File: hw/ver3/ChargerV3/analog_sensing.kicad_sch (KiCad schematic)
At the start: 34 parts, among them U16 ADS1220xPW, U17 74HC4051PW, U18 74HC4051PW

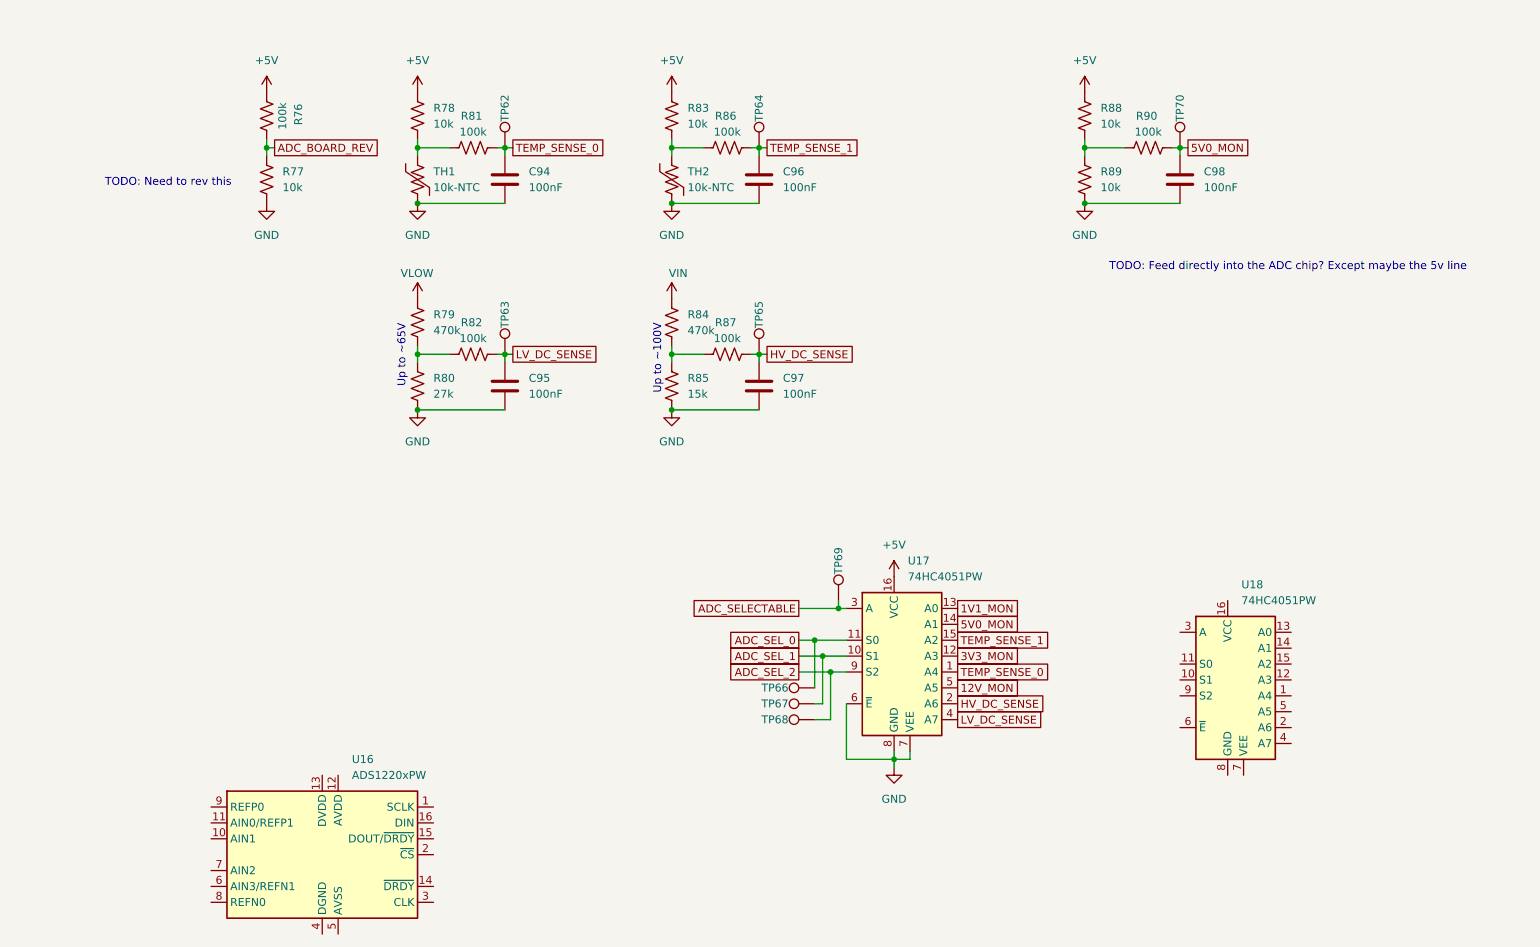
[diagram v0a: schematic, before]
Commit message: Split the design into four major components. Start working on system architecture.
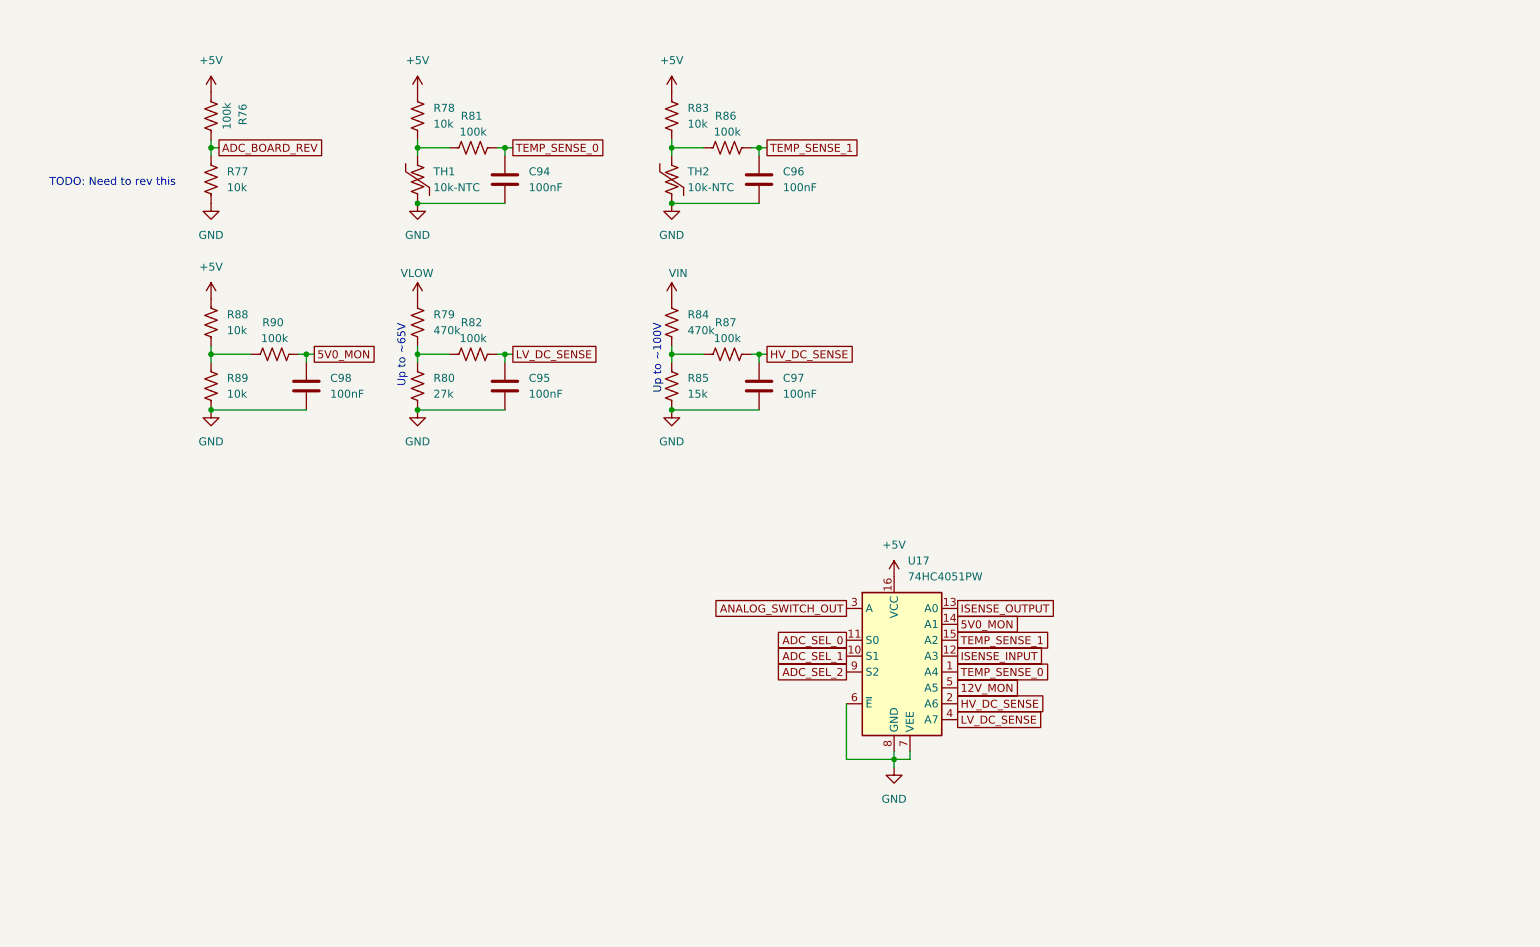
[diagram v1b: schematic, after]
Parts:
- removed TP62, TP63, TP64, TP65, TP66, TP67, TP68, TP69, TP70: TestPoint, TestPoint:TestPoint_Pad_D1.0mm, symbol Connector:TestPoint
- removed U16: ADS1220xPW, Package_SO:TSSOP-16_4.4x5mm_P0.65mm, symbol Analog_ADC:ADS1220xPW
- removed U18: 74HC4051PW, Package_SO:TSSOP-16_4.4x5mm_P0.65mm, symbol 74xx:74HC4051
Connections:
- net 1V1_MON renamed ISENSE_OUTPUT
- net 3V3_MON renamed ISENSE_INPUT
- net ADC_SELECTABLE renamed ANALOG_SWITCH_OUT
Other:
- note removed: "TODO: Feed directly into the ADC chip? Except maybe the 5v line"
- moved on the sheet: C98, R76, R77, R88, R89, R90

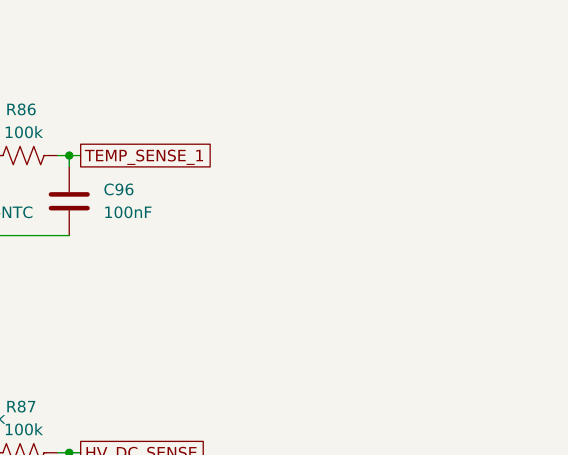
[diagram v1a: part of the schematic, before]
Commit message: Redo some charger routing. Improve design for interconnect
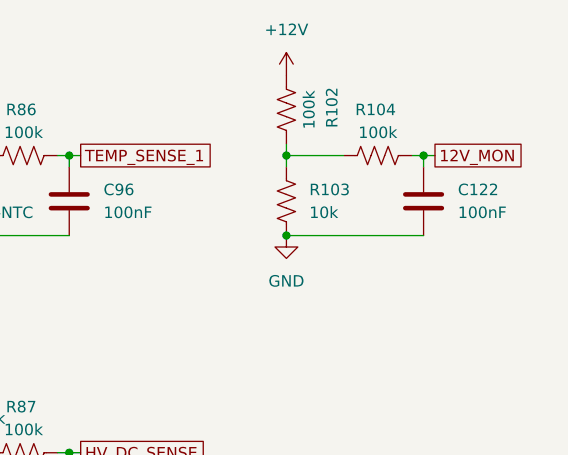
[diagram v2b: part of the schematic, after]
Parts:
- added C122: 100nF, Capacitor_SMD:C_0603_1608Metric, symbol Device:C
- added R102, R104: 100k, Resistor_SMD:R_0603_1608Metric, symbol Device:R_US
- added R103: 10k, Resistor_SMD:R_0603_1608Metric, symbol Device:R_US
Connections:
- net 12V_MON: now also C122.1, R104.2
- net GND: now also C122.2, R103.1
- new net: R102.2, R103.2, R104.1
- new net +12V: R102.1

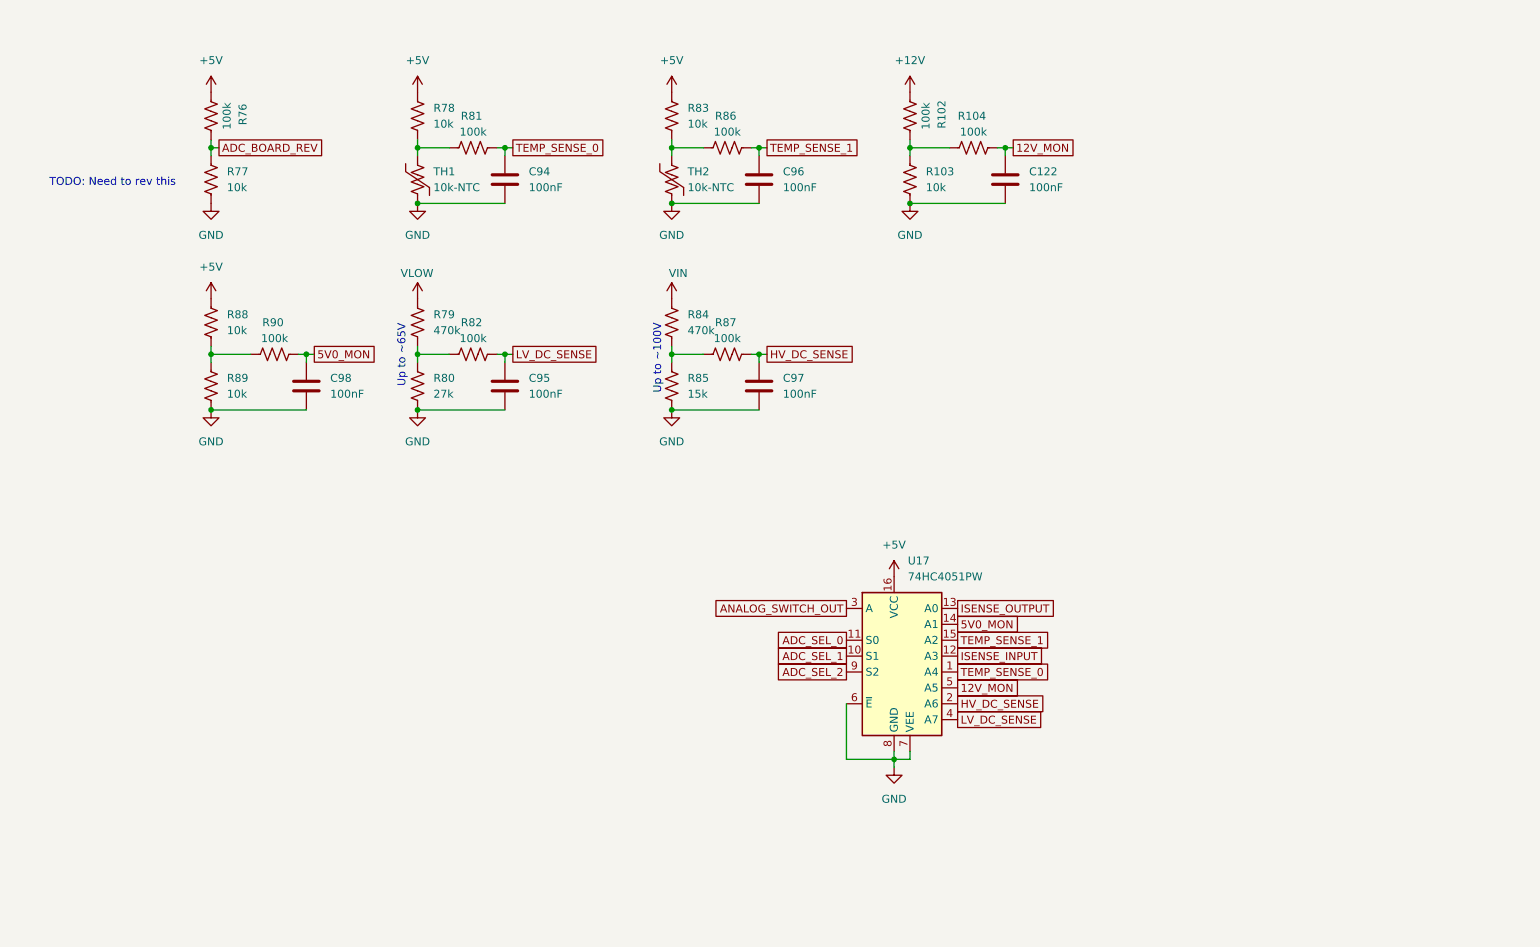
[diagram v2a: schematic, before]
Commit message: Nearly final charger schematic, updated with RS485 interconnect.
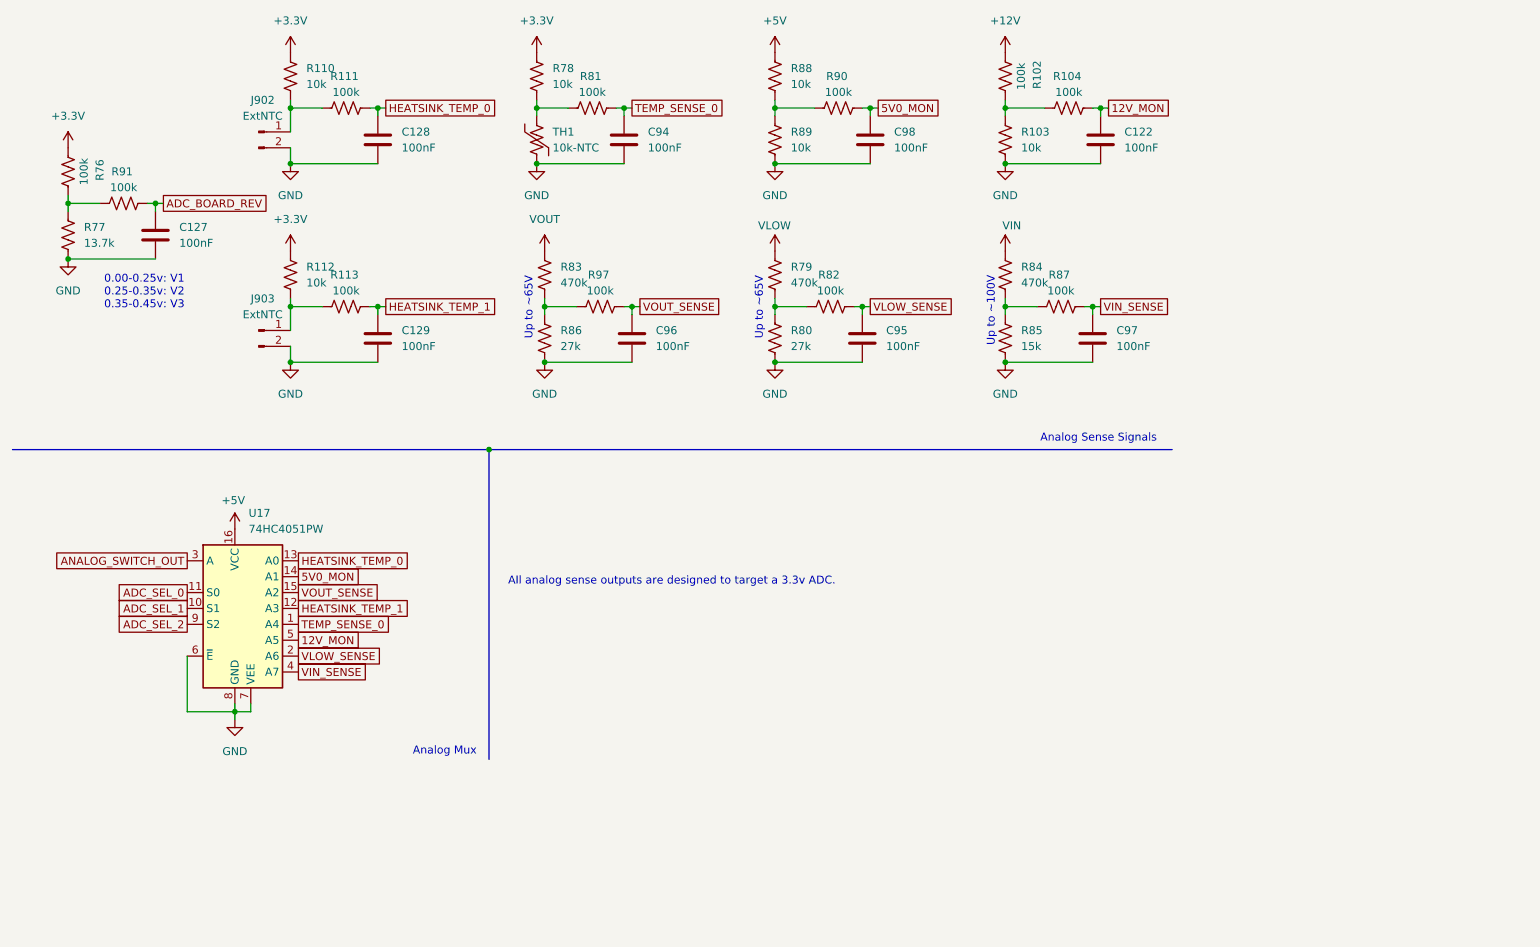
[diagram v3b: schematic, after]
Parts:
- removed TH2: 10k-NTC, Resistor_SMD:R_0402_1005Metric_Pad0.72x0.64mm_HandSolder, symbol Device:Thermistor_US
- added C127, C128, C129: 100nF, Capacitor_SMD:C_0603_1608Metric, symbol Device:C
- added J902, J903: ExtNTC, Connector_PinHeader_2.54mm:PinHeader_1x02_P2.54mm_Vertical, symbol Connector:Conn_01x02_Pin
- added R110, R112: 10k, Resistor_SMD:R_0603_1608Metric, symbol Device:R_US
- added R111, R113, R91, R97: 100k, Resistor_SMD:R_0603_1608Metric, symbol Device:R_US
- R77: value 10k -> 13.7k; LCSC C25804 -> C2930064
- R83: value 10k -> 470k; footprint Resistor_SMD:R_0603_1608Metric -> Resistor_SMD:R_0805_2012Metric; LCSC C25804 -> C17709
- R86: value 100k -> 27k; LCSC C25803 -> C22967
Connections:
- net +5V: no longer R76.1, R78.2, R83.2
- net ADC_BOARD_REV: now also C127.1, R91.2; no longer R76.2, R77.2
- net GND: now also R86.1, C127.2, C128.2, C129.2, J902.2 (Pin_2), J903.2 (Pin_2)
- net at R83.1: now also R86.2, R97.1; no longer R86.1
- net HV_DC_SENSE renamed VIN_SENSE
- net VIN_SENSE: now also U17.4 (A7); no longer U17.2 (A6)
- net ISENSE_INPUT renamed HEATSINK_TEMP_1
- net HEATSINK_TEMP_1: now also C129.1, R113.2
- net ISENSE_OUTPUT renamed HEATSINK_TEMP_0
- net HEATSINK_TEMP_0: now also C128.1, R111.2
- net LV_DC_SENSE renamed VLOW_SENSE
- net VLOW_SENSE: now also U17.2 (A6); no longer U17.4 (A7)
- net TEMP_SENSE_1 renamed VOUT_SENSE
- net VOUT_SENSE: now also R97.2; no longer R86.2
- new net: J902.1 (Pin_1), R110.1, R111.1
- new net: R76.2, R77.2, R91.1
- new net: J903.1 (Pin_1), R112.1, R113.1
- new net +3.3V: R110.2, R112.2, R76.1, R78.2
- new net VOUT: R83.2
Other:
- note added: "0.00-0.25v: V1 0.25-0.35v: V2 0.35-0.45v: V3"
- note added: "All analog sense outputs are designed to target a 3.3v ADC."
- note added: "Analog Mux"
- note added: "Analog Sense Signals"
- note removed: "TODO: Need to rev this"
- moved on the sheet: C122, C94, C95, C97, C98, R102, R103, R104, R76, R77, R78, R79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
